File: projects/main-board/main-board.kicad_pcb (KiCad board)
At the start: 4 copper layers, 215 parts, among them J1 TC2030, J2 TC2030, J3 S3B-PH-SM4-TB, J4 USB4105-GF-A, J5 TC2030, J6 NHD-4.3-480272EF-ASXP (Molex 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, J7 USB4105-GF-A, Q1 ZXTN4240F-7, Q2 ZXTN4240F-7, SW1 450404015514, SW10 TS06-667-25-BK-160-G-SMT-TR, SW11 TS06-667-25-BK-160-G-SMT-TR, SW12 TS06-667-25-BK-160-G-SMT-TR, SW13 TS06-667-25-BK-160-G-SMT-TR, SW14 TS06-667-25-BK-160-G-SMT-TR, SW15 TS06-667-25-BK-160-G-SMT-TR, SW16 TS06-667-25-BK-160-G-SMT-TR, SW18 TS06-667-25-BK-160-G-SMT-TR, SW2 TS06-667-25-BK-160-G-SMT-TR, SW3 TS06-667-25-BK-160-G-SMT-TR, SW4 TS06-667-25-BK-160-G-SMT-TR, SW5 TS06-667-25-BK-160-G-SMT-TR, SW6 TS06-667-25-BK-160-G-SMT-TR, SW7 TS06-667-25-BK-160-G-SMT-TR, SW8 TS06-667-25-BK-160-G-SMT-TR, SW9 TS06-667-25-BK-160-G-SMT-TR, U1 STM32N657X0HxQ, U10 AP5725WG-7, U11 NAU8325YG, U12 TLV74330PDBVR, U13 DM3AT-SF-PEJM5, U14 LSM6DSO32TR, U2 APS256XXN-OBR-BG, U3 MX25UM25645GXDI00, U4 TPS22992RXPR, U5 MPM3805GQB-18-Z, U6 TPSM863253RDXR, U7 MAX77972EWX+T, U8 TS3USB221ARSER, U9 ESP32-C6FH4, Y1 ABM10W-40.0000MHZ-8-B1U-T3

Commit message: Update render.
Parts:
- removed SW15, SW16, SW7, SW8: TS06-667-25-BK-160-G-SMT-TR, footprint-library:TS06-667-25-BK-160-G-SMT-TR
- SW10, SW11, SW12, SW13, SW14, SW18, SW2, SW3, SW4, SW5, SW6, SW9: moved to B.Cu
- moved SW3 187.6 mm to (222.6, 77.7), turned to 180 degrees
- moved SW14 174.9 mm to (91.4, 76.5), turned to 180 degrees
- moved SW10 168.5 mm to (82.4, 84.2), turned to 180 degrees
- moved SW11 168.4 mm to (83.0, 69.5), turned to 180 degrees
- moved SW6 168.2 mm to (214.2, 70.2), turned to 180 degrees
- moved SW12 166.5 mm to (215.6, 58.8), turned to 0 degrees
- moved SW18 154.6 mm to (99.4, 53.6), turned to 0 degrees
- moved SW2 149.6 mm to (206.1, 77.7), turned to 180 degrees
- moved SW5 131.6 mm to (82.9, 57.7), turned to 180 degrees
- moved R41 85.5 mm to (100.1, 51.4), turned to 90 degrees
- moved R42 85.0 mm to (101.1, 51.4), turned to 90 degrees
- moved R43 84.5 mm to (102.1, 51.4), turned to 90 degrees
- moved C53 83.9 mm to (103.6, 51.5), turned to 90 degrees
- moved C54 83.5 mm to (104.5, 51.5), turned to 90 degrees
- moved C55 83.0 mm to (105.5, 51.5), turned to 90 degrees
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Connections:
- SW10 pad 1: /Buttons/BUTTONS.B9 -> /Buttons/BUTTONS.B7
- SW10 pad 3: /Buttons/BUTTONS.B9 -> /Buttons/BUTTONS.B7
- SW11 pad 1: /Buttons/BUTTONS.B10 -> /Buttons/BUTTONS.B8
- SW11 pad 3: /Buttons/BUTTONS.B10 -> /Buttons/BUTTONS.B8
- SW12 pad 1: /Buttons/BUTTONS.B11 -> /Buttons/BUTTONS.B9
- SW12 pad 3: /Buttons/BUTTONS.B11 -> /Buttons/BUTTONS.B9
- SW13 pad 1: /Buttons/BUTTONS.B12 -> /Buttons/BUTTONS.B10
- SW13 pad 3: /Buttons/BUTTONS.B12 -> /Buttons/BUTTONS.B10
- SW14 pad 1: /Buttons/BUTTONS.B13 -> /Buttons/BUTTONS.B11
- SW14 pad 3: /Buttons/BUTTONS.B13 -> /Buttons/BUTTONS.B11
- SW9 pad 1: /Buttons/BUTTONS.B8 -> /Buttons/BUTTONS.B6
- SW9 pad 3: /Buttons/BUTTONS.B8 -> /Buttons/BUTTONS.B6
- U1 pad N1: /Buttons/BUTTONS.B15 -> unconnected-(U1F-PF15-PadN1)
- U1 pad N2: /Buttons/BUTTONS.B14 -> unconnected-(U1F-PF14-PadN2)
- U1 pad R2: /Buttons/BUTTONS.B13 -> unconnected-(U1F-PF13-PadR2)
- U1 pad T1: /Buttons/BUTTONS.B12 -> unconnected-(U1F-PF12-PadT1)
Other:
- board outline added: 165 x 68 mm

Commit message: Update render
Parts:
- removed SW13, SW14: TS06-667-25-BK-160-G-SMT-TR, footprint-library:TS06-667-25-BK-160-G-SMT-TR
- C1, C10, C11, C12, C13, C14, C15, C16, C17, C18, C19, C2, C20, C21, C22, C23, C24, C25, C26, C27, C28, C29, C3, C30, C31, C32, C33, C34, C35, C36, C37, C38, C39, C4, C40, C41, C42, C43, C44, C45, C46, C47, C48, C5, C6, C7, C8, C89, C9, C90, L1, L2, L3, R1, R2, R3, R4, R5, R6, R7, R8: moved to B.Cu
- moved U13 121.3 mm to (220.4, 74.8), turned to 90 degrees
- moved R60 114.7 mm to (210.4, 80.7)
- moved C104 109.6 mm to (210.2, 75.4), turned to 180 degrees
- moved C105 108.7 mm to (210.2, 74.4), turned to 180 degrees
- moved SW1 97.7 mm to (128.9, 39.9), turned to 0 degrees
- moved J3 77.8 mm to (113.0, 98.6), turned to 90 degrees
- moved C16 66.6 mm to (162.5, 67.9), turned to 0 degrees
- moved C24 65.5 mm to (162.5, 66.4), turned to 0 degrees
- moved C29 65.0 mm to (161.4, 66.9), turned to 0 degrees
- moved L3 64.5 mm to (162.6, 64.8), turned to 0 degrees
- moved C32 63.4 mm to (162.4, 63.1), turned to 0 degrees
- moved C39 62.8 mm to (162.4, 61.9), turned to 0 degrees
- moved C87 62.3 mm to (188.1, 76.4)
- moved C88 62.3 mm to (196.2, 80.3)
- moved D1 62.3 mm to (194.6, 79.5)
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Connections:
- U1 pad L4: /Buttons/BUTTONS.B10 -> unconnected-(U1F-PF10-PadL4)
- U1 pad P3: /Buttons/BUTTONS.B11 -> unconnected-(U1F-PF11-PadP3)
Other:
- board size 165 x 68 mm -> 165 x 77 mm

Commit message: Update PCB profile and render
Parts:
- moved C105 27.3 mm to (220.7, 99.7)
- moved R60 27.3 mm to (220.9, 105.9)
- moved U13 27.3 mm to (230.9, 100.1)
- moved C104 27.3 mm to (220.7, 100.6)
- moved SW9 27.0 mm to (221.8, 105.8)
- moved SW10 26.7 mm to (81.4, 108.3)
- moved C53 26.5 mm to (117.8, 77.8)
- moved C55 26.5 mm to (117.8, 75.8)
- moved C56 26.5 mm to (117.8, 74.9)
- moved C54 26.5 mm to (117.8, 76.8)
- moved C57 26.5 mm to (117.8, 73.9)
- moved C58 26.5 mm to (117.8, 72.9)
- moved SW12 26.1 mm to (216.8, 74.8)
- moved R41 26.0 mm to (117.8, 80.8)
- moved R42 26.0 mm to (117.8, 79.8)
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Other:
- board size 165 x 77 mm -> 174 x 75.9 mm

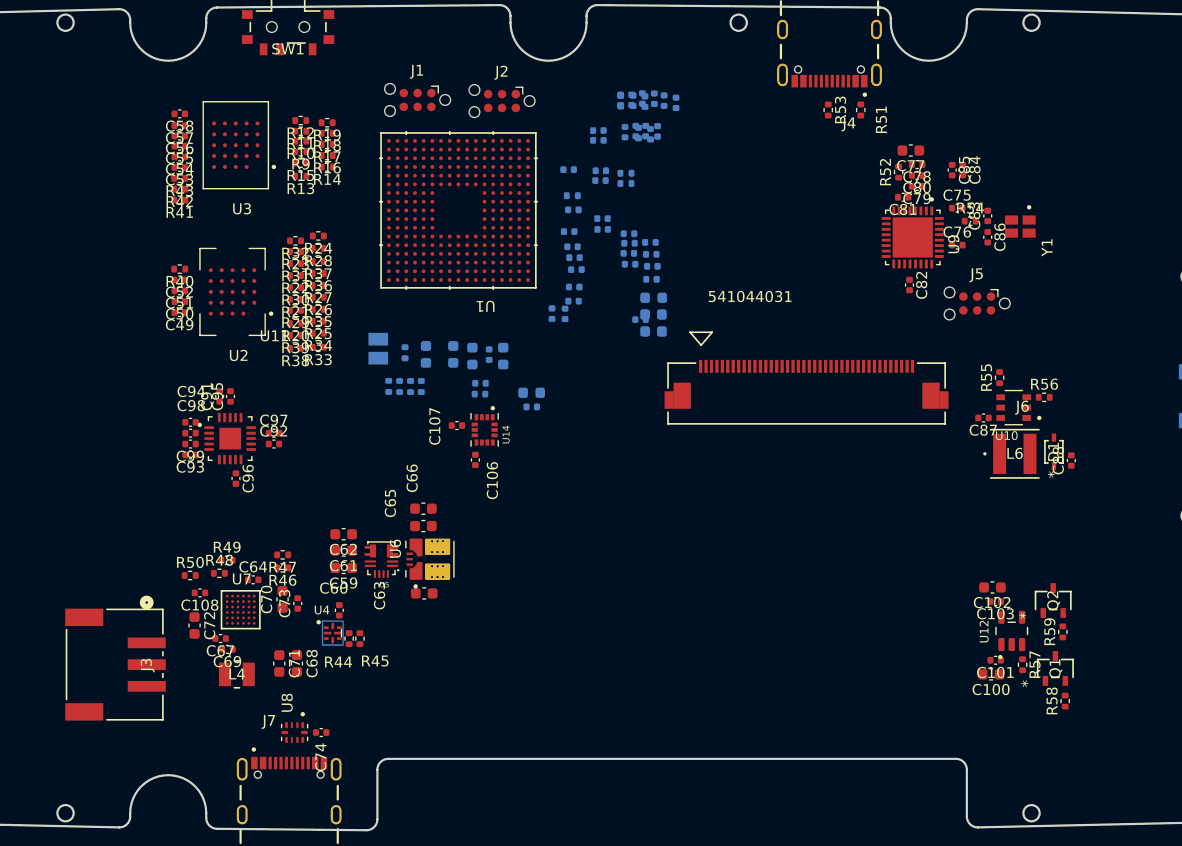
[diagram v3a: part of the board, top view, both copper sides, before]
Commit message: Main board PCB layout and routing
- Add 48MHz crystal for STM32
- Add 32kHz crystal for STM32
- Started laying out and routing board
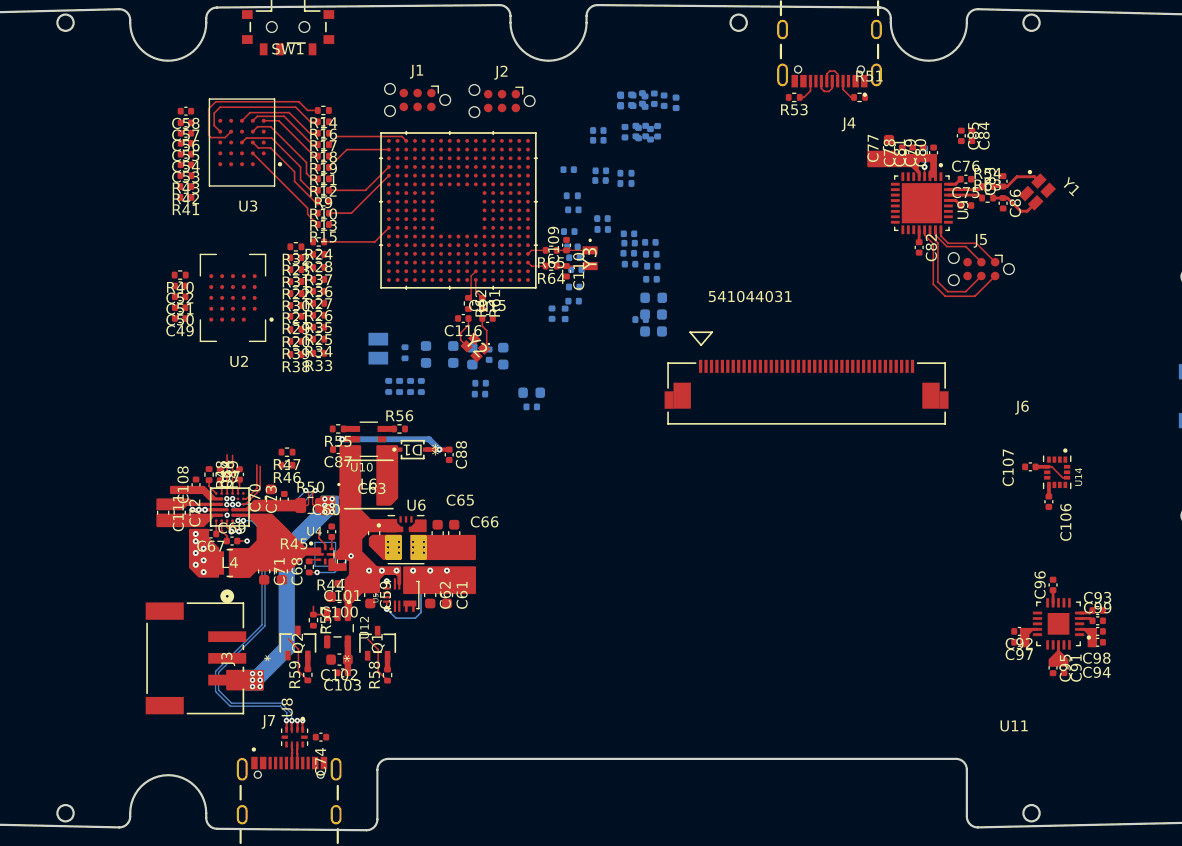
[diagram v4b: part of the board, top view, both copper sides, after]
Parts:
- added C109: 9pF 50V, Capacitor_SMD:C_0402_1005Metric, F.Cu at (153.4, 84.9)
- added C110: 9pF 50V, Capacitor_SMD:C_0402_1005Metric, F.Cu at (153.4, 87.4)
- added C111: 22uF 10V, Capacitor_SMD:C_0603_1608Metric, F.Cu at (116.3, 109.6)
- added C115: 8pF 50V, Capacitor_SMD:C_0402_1005Metric, F.Cu at (146.1, 91.7)
- added C116: 8pF 50V, Capacitor_SMD:C_0402_1005Metric, F.Cu at (143.9, 91.7)
- added R61: 0R, Resistor_SMD:R_0402_1005Metric, F.Cu at (145.7, 90.3)
- added R62: 0R, Resistor_SMD:R_0402_1005Metric, F.Cu at (144.4, 90.3)
- added R63: 0R, Resistor_SMD:R_0402_1005Metric, F.Cu at (192.2, 80.6)
- added R64: 0R, Resistor_SMD:R_0402_1005Metric, F.Cu at (152.0, 86.9)
- added R65: 0R, Resistor_SMD:R_0402_1005Metric, F.Cu at (152.0, 85.4)
- added Y2: ABM11W-48.0000MHZ-8-K1Z-T3, footprint-library:ABM11W300000MHZ4B1UT3, F.Cu at (145.0, 94.4)
- added Y3: ABS06-32.768KHZ-9-1-T, footprint-library:ABS06, F.Cu at (155.6, 86.2)
- R50: footprint Resistor_SMD:R_0402_1005Metric -> Resistor_SMD:R_0805_2012Metric
- R52: moved to B.Cu
- moved C94 85.9 mm to (202.3, 121.5), turned to 0 degrees
- moved C98 85.5 mm to (202.3, 120.5), turned to 0 degrees
- moved C99 85.1 mm to (202.3, 119.5), turned to 0 degrees
- moved C93 84.7 mm to (202.3, 118.6), turned to 0 degrees
- moved C91 81.6 mm to (199.2, 123.9), turned to -90 degrees
- moved C95 79.7 mm to (198.2, 123.9), turned to -90 degrees
- moved U11 78.1 mm to (198.7, 119.8), turned to 180 degrees
- moved C96 75.8 mm to (198.2, 116.2), turned to 90 degrees
- moved C97 71.3 mm to (195.1, 121.5), turned to 180 degrees
- moved C92 70.7 mm to (195.1, 120.5), turned to 180 degrees
- moved Q2 69.6 mm to (128.7, 121.6)
- moved R59 69.6 mm to (129.6, 124.5)
- moved R57 65.4 mm to (130.1, 119.5)
- moved Q1 62.4 mm to (136.0, 121.6)
- moved R58 62.4 mm to (136.9, 124.5)
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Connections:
- C77 pad 1: Net-(C77-Pad1) -> 3V3
- C78 pad 1: Net-(C77-Pad1) -> 3V3
- C79 pad 1: Net-(C77-Pad1) -> 3V3
- C80 pad 1: Net-(C77-Pad1) -> 3V3
- C81 pad 1: Net-(U9-VDDPST1) -> 3V3
- C82 pad 1: Net-(U9-VDDPST1) -> 3V3
- C86 pad 1: Net-(U9-XTAL_N) -> Net-(C86-Pad1)
- U1 pad A5: /MCU/USB.DM -> /MCU/USB.DN
- U1 pad A7: unconnected-(U1H-PH0-OSC_IN(PH0)-PadA7) -> Net-(U1H-PH0-OSC_IN(PH0))
- U1 pad B7: unconnected-(U1H-PH1-OSC_OUT(PH1)-PadB7) -> Net-(U1H-PH1-OSC_OUT(PH1))
- U1 pad C1: unconnected-(U1C-PC15-OSC32_OUT(OSC32_OUT)-PadC1) -> Net-(U1C-PC15-OSC32_OUT(OSC32_OUT))
- U1 pad D1: unconnected-(U1C-PC14-OSC32_IN(OSC32_IN)-PadD1) -> Net-(U1C-PC14-OSC32_IN(OSC32_IN))
- U12 pad 4: unconnected-(U12-NC-Pad4) -> GND
- U8 pad 1: /USB Switch/USB_DOWN_1.DP -> /MCU/USB.DP
- U8 pad 2: /USB Switch/USB_DOWN_1.DN -> /MCU/USB.DN
- U9 pad 2: Net-(C77-Pad1) -> 3V3
- U9 pad 20: Net-(U9-VDDPST1) -> 3V3
- U9 pad 3: Net-(C77-Pad1) -> 3V3
- U9 pad 5: Net-(U9-VDDPST1) -> 3V3
- Y1 pad 3: Net-(U9-XTAL_N) -> Net-(C86-Pad1)
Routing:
- net VBAT: track 0.00 -> 29.9 mm, vias 0 -> 14
- net /Power/USB.DP: track 0.00 -> 29.0 mm, vias 0 -> 2
- net /Power/USB.DN: track 0.00 -> 27.6 mm, vias 0 -> 2
- net /Flash/FLASH_OCTOSPI.SIO3: track 0.00 -> 15.5 mm
- net BACKLIGHT_P: track 0.00 -> 12.6 mm, vias 0 -> 2
- net /ESP32/ESP32_UART.TX: track 0.00 -> 12.3 mm
- net /Flash/FLASH_OCTOSPI.SIO4: track 0.00 -> 12.3 mm
- net 3V3: track 0.00 -> 10.8 mm
- net /ESP32/ESP32_UART.RX: track 0.00 -> 10.1 mm
- net /Flash/FLASH_OCTOSPI.DQS: track 0.00 -> 9.84 mm
- net 1V8: track 0.00 -> 9.66 mm, vias 0 -> 4
- net /Flash/FLASH_OCTOSPI.SCLK: track 0.00 -> 9.03 mm
- net Net-(U7-CSP): track 0.00 -> 8.89 mm, vias 0 -> 2
- net /Flash/FLASH_OCTOSPI.CS_N: track 0.00 -> 8.75 mm
- net /Flash/FLASH_OCTOSPI.SIO1: track 0.00 -> 8.75 mm
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
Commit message: PCB layout and renders
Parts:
- C49, C50, C51, C52, C53, C54, C55, C56, C57, C58, R40, R41, R42, R43: moved to B.Cu
- U4: value TPS22992RXPR -> TPS22992RXPR
- U7: value MAX77972EWX+T -> 21-100517_W363B3+1_ADI
- moved C92 59.7 mm to (136.9, 107.1)
- moved C96 59.7 mm to (140.0, 102.8)
- moved C97 59.7 mm to (136.9, 108.1)
- moved C98 59.7 mm to (144.1, 107.1)
- moved C93 59.7 mm to (144.1, 105.2)
- moved C95 59.7 mm to (140.0, 110.5)
- moved C99 59.7 mm to (144.1, 106.2)
- moved C91 59.7 mm to (141.0, 110.5)
- moved U11 59.7 mm to (140.5, 106.4)
- moved C94 59.7 mm to (144.1, 108.1)
- moved C106 41.1 mm to (156.7, 109.2)
- moved U14 41.1 mm to (157.5, 106.5)
- moved C107 41.1 mm to (155.0, 106.0)
- moved L6 24.2 mm to (153.7, 122.7)
- moved R55 24.2 mm to (150.9, 117.6)
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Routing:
- net /Power/USB.DP: track 29.0 -> 4.85 mm
- net /Power/USB.DN: track 27.6 -> 3.73 mm
- net /Flash/FLASH_OCTOSPI.RESET_N: track 0.00 -> 17.4 mm, vias 0 -> 2
- net 1V8: track 9.66 -> 24.5 mm, vias 4 -> 9
- net VBAT: track 29.9 -> 15.4 mm, vias 14 -> 2
- net Net-(U1I-PN6): track 0.00 -> 14.1 mm
- net Net-(U1L-PP5): track 0.00 -> 12.6 mm, vias 0 -> 2
- net /MCU/RAM_HEXASPI.CS_N: track 0.00 -> 12.4 mm, vias 0 -> 1
- net /MCU/RAM_HEXASPI.D9: track 0.00 -> 12.0 mm
- net Net-(U1I-PN3): track 0.00 -> 11.8 mm
- net /MCU/RAM_HEXASPI.D7: track 0.00 -> 11.8 mm
- net /MCU/RAM_HEXASPI.D10: track 0.00 -> 11.7 mm
- net Net-(U1L-PP4): track 0.00 -> 11.3 mm, vias 0 -> 2
- net Net-(U1I-PN11): track 0.00 -> 11.0 mm
- net Net-(U1I-PN5): track 0.00 -> 10.8 mm
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
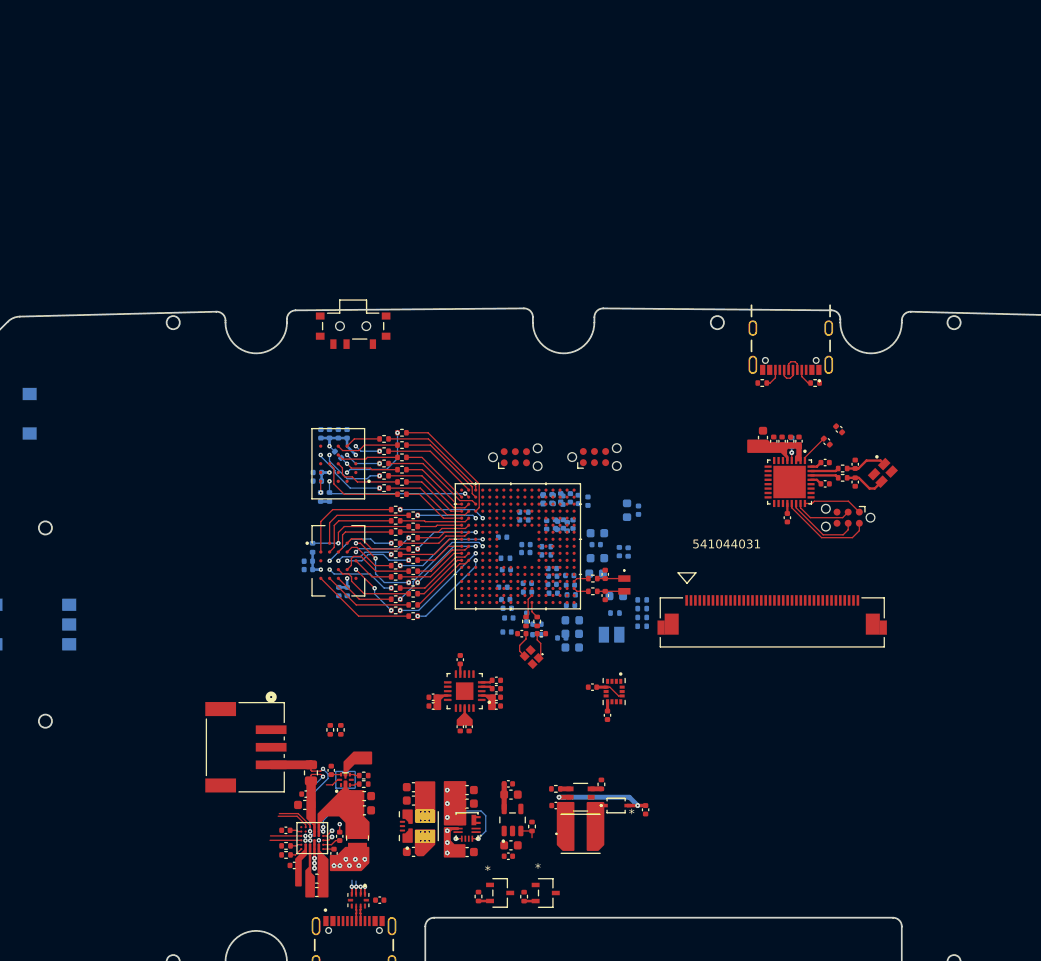
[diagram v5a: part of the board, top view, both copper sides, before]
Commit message: Routed LCD signals
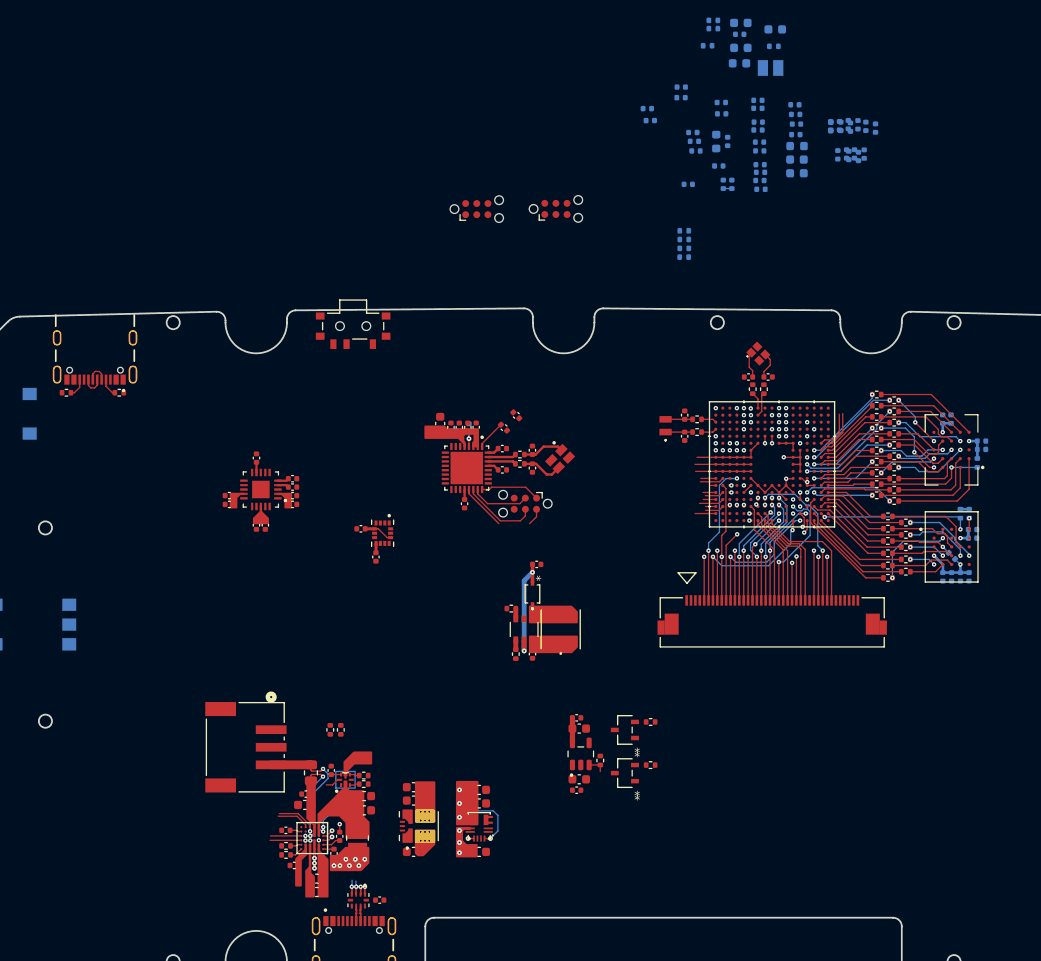
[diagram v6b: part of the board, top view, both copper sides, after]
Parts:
- U4: value TPS22992RXPR -> TPS22992RXPR
- U7: value 21-100517_W363B3+1_ADI -> MAX77972EWX+T
- moved R51 79.2 mm to (101.2, 72.5)
- moved J4 79.2 mm to (98.4, 66.2)
- moved R53 79.2 mm to (95.1, 72.5)
- moved C52 78.0 mm to (199.3, 78.0), turned to 0 degrees
- moved C49 77.7 mm to (199.3, 78.9), turned to 0 degrees
- moved R40 76.3 mm to (198.8, 80.5), turned to -90 degrees
- moved C58 75.6 mm to (197.9, 93.4), turned to -90 degrees
- moved C53 75.0 mm to (198.3, 89.0), turned to 0 degrees
- moved C56 74.8 mm to (198.3, 88.0), turned to 0 degrees
- moved R43 73.9 mm to (197.9, 86.2), turned to -90 degrees
- moved C55 73.7 mm to (196.9, 93.4), turned to -90 degrees
- moved C50 72.4 mm to (195.8, 75.5), turned to 90 degrees
- moved R42 71.9 mm to (196.9, 86.2), turned to -90 degrees
- moved C57 71.7 mm to (195.9, 93.4), turned to -90 degrees
- moved U2 70.9 mm to (195.9, 79.0), turned to 180 degrees
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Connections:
- C12 pad 1: VBAT -> Net-(U1K-VBAT)
- U1 pad A13: unconnected-(U1D-PD10-PadA13) -> /ESP32/ESP32_GPIO.3
- U1 pad A14: /MCU/PMIC_STATUS -> /ESP32/ESP32_GPIO.9
- U1 pad A8: /ESP32/ESP32_GPIO.9 -> unconnected-(U1C-PC10-PadA8)
- U1 pad A9: /ESP32/ESP32_GPIO.3 -> unconnected-(U1C-PC1-PadA9)
- U1 pad B1: /LCD/LCD.B4 -> unconnected-(U1H-PH3-PadB1)
- U1 pad B14: /LCD/LCD.R2 -> unconnected-(U1D-PD15-PadB14)
- U1 pad B17: /LCD/LCD.HSYNC -> unconnected-(U1B-PB14-PadB17)
- U1 pad B2: /LCD/LCD.B5 -> unconnected-(U1H-PH6-PadB2)
- U1 pad C12: /MCU/PMIC_INPUT_VALID -> unconnected-(U1D-PD2-PadC12)
- U1 pad C14: unconnected-(U1D-PD14-PadC14) -> /MCU/DEBUG_UART.RX
- U1 pad C15: /LCD/LCD.CLK -> unconnected-(U1B-PB13-PadC15)
- U1 pad C16: /LCD/LCD.B2 -> unconnected-(U1B-PB2-PadC16)
- U1 pad D13: /MCU/PMIC_ALERT -> unconnected-(U1D-PD0-PadD13)
- U1 pad D15: unconnected-(U1B-PB9-PadD15) -> /MCU/DEBUG_UART.TX
- U1 pad D17: /LCD/LCD.G4 -> unconnected-(U1B-PB15-PadD17)
- U1 pad D3: /LCD/LCD.EN -> unconnected-(U1M-PQ3-PadD3)
- U1 pad D5: unconnected-(U1M-PQ5-PadD5) -> /MCU/LEFT_MOTOR_PWM
- U1 pad E13: /MCU/PMIC_CHARGE_EN -> unconnected-(U1D-PD3-PadE13)
- U1 pad E14: /LCD/LCD.R7 -> unconnected-(U1D-PD8-PadE14)
- U1 pad F4: /LCD/LCD.R4 -> /Buttons/BUTTONS.B3
- U1 pad G5: unconnected-(U1M-PQ7-PadG5) -> /MCU/RIGHT_MOTOR_PWM
- U1 pad H14: /LCD/LCD.R1 -> unconnected-(U1D-PD9-PadH14)
- U1 pad L1: unconnected-(U1G-PG7-PadL1) -> /Buttons/BUTTONS.B6
- U1 pad L3: /LCD/LCD.B3 -> unconnected-(U1G-PG6-PadL3)
- U1 pad L4: unconnected-(U1F-PF10-PadL4) -> /LCD/LCD.R1
- U1 pad L5: /Buttons/BUTTONS.B6 -> unconnected-(U1F-PF6-PadL5)
- U1 pad M2: /Buttons/BUTTONS.B3 -> /LCD/LCD.R4
- U1 pad N1: unconnected-(U1F-PF15-PadN1) -> /MCU/PMIC_INPUT_VALID
- U1 pad N2: unconnected-(U1F-PF14-PadN2) -> /MCU/PMIC_STATUS
- U1 pad N4: /Buttons/BUTTONS.B2 -> unconnected-(U1F-PF2-PadN4)
- U1 pad P2: unconnected-(U1G-PG4-PadP2) -> /Buttons/BUTTONS.B2
- U1 pad P4: /Buttons/BUTTONS.B1 -> unconnected-(U1F-PF1-PadP4)
- U1 pad P7: /MCU/DEBUG_UART.TX -> /LCD/LCD.B5
- U1 pad P8: /MCU/RIGHT_MOTOR_PWM -> /LCD/LCD.HSYNC
- U1 pad R1: unconnected-(U1G-PG3-PadR1) -> /MCU/PMIC_CHARGE_EN
- U1 pad R2: unconnected-(U1F-PF13-PadR2) -> /MCU/PMIC_ALERT
- U1 pad R7: /MCU/DEBUG_UART.RX -> /LCD/LCD.B4
- U1 pad R8: /MCU/LEFT_MOTOR_PWM -> /LCD/LCD.CLK
- U1 pad T1: unconnected-(U1F-PF12-PadT1) -> /Buttons/BUTTONS.B1
- U1 pad T10: unconnected-(U1G-PG10-PadT10) -> /LCD/LCD.G4
- U1 pad T13: unconnected-(U1G-PG9-PadT13) -> /LCD/LCD.R7
- U1 pad T7: unconnected-(U1A-PA11-PadT7) -> /LCD/LCD.B3
- U1 pad U12: unconnected-(U1B-PB5(JTDO/TRACESWO)-PadU12) -> /LCD/LCD.R2
- U1 pad U14: unconnected-(U1A-PA4-PadU14) -> /LCD/LCD.EN
- U1 pad U7: unconnected-(U1A-PA12-PadU7) -> /LCD/LCD.B2
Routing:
- net /LCD/LCD.R0: track 0.00 -> 25.2 mm, vias 0 -> 2
- net /LCD/LCD.VSYNC: track 0.00 -> 23.0 mm, vias 0 -> 2
- net /LCD/LCD.R7: track 0.00 -> 18.2 mm, vias 0 -> 2
- net /LCD/LCD.R2: track 0.00 -> 18.0 mm, vias 0 -> 2
- net /LCD/LCD.R5: track 0.00 -> 17.2 mm, vias 0 -> 2
- net /LCD/LCD.HSYNC: track 0.00 -> 17.2 mm, vias 0 -> 2
- net /LCD/LCD.R3: track 0.00 -> 16.6 mm, vias 0 -> 2
- net /LCD/LCD.R6: track 0.00 -> 16.0 mm, vias 0 -> 2
- net /LCD/LCD.R1: track 0.00 -> 15.9 mm, vias 0 -> 2
- net /LCD/LCD.G2: track 0.00 -> 15.0 mm, vias 0 -> 2
- net /LCD/LCD.B1: track 0.00 -> 14.2 mm, vias 0 -> 2
- net /LCD/LCD.CLK: track 0.00 -> 14.1 mm, vias 0 -> 2
- net /LCD/LCD.DE: track 0.00 -> 14.1 mm
- net /LCD/LCD.B5: track 0.00 -> 13.5 mm, vias 0 -> 2
- net /LCD/LCD.R4: track 0.00 -> 13.4 mm, vias 0 -> 1
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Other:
- copper layers 4 -> 6
